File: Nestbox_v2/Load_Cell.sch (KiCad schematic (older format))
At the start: 29 parts

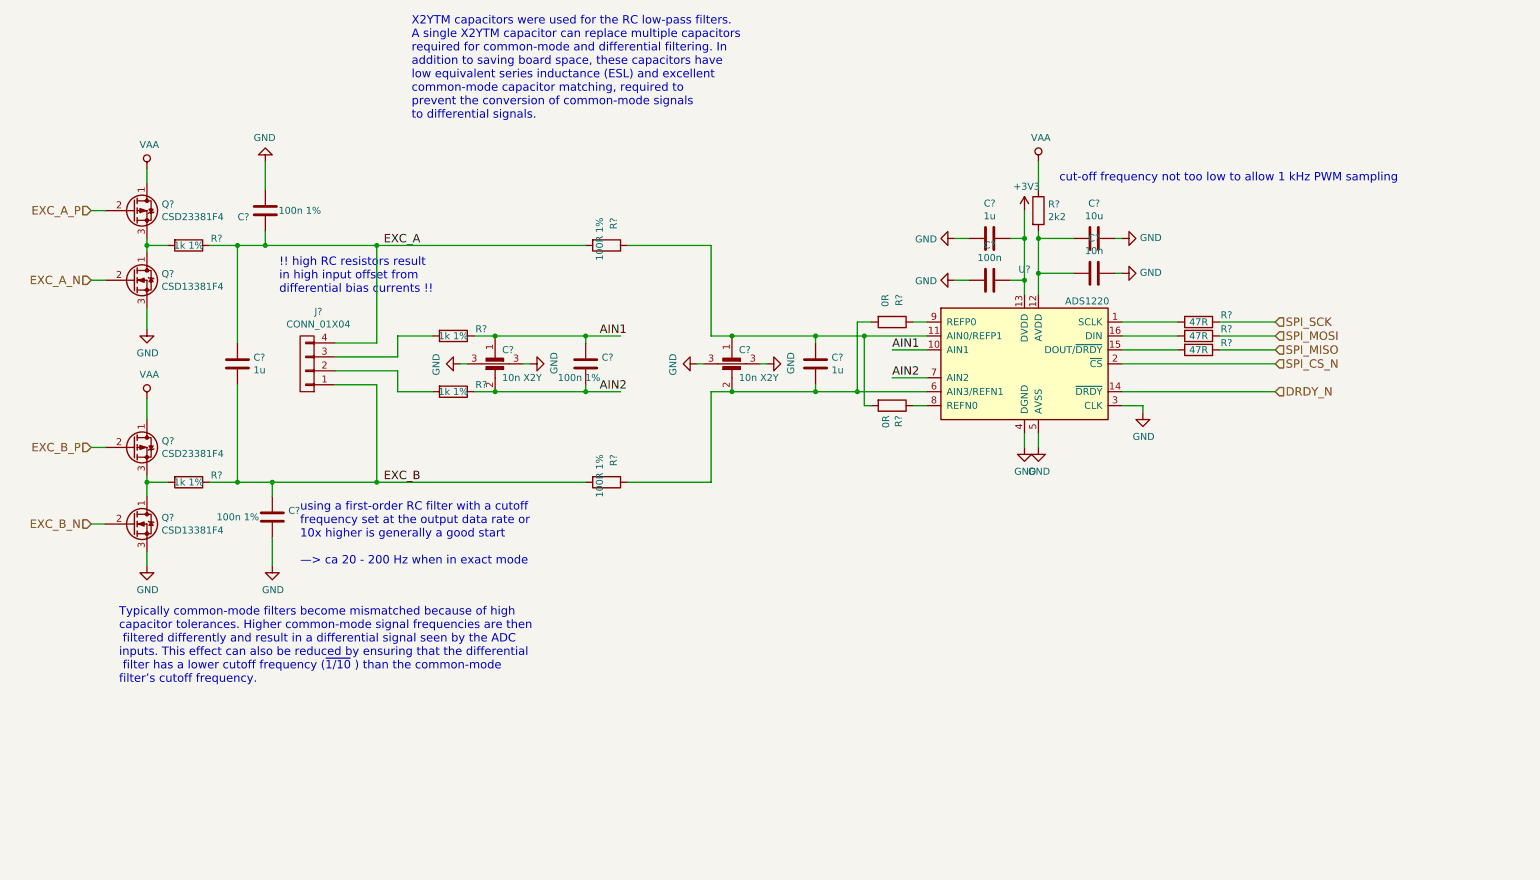
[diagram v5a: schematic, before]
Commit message: added PIR and lightbarrier headers
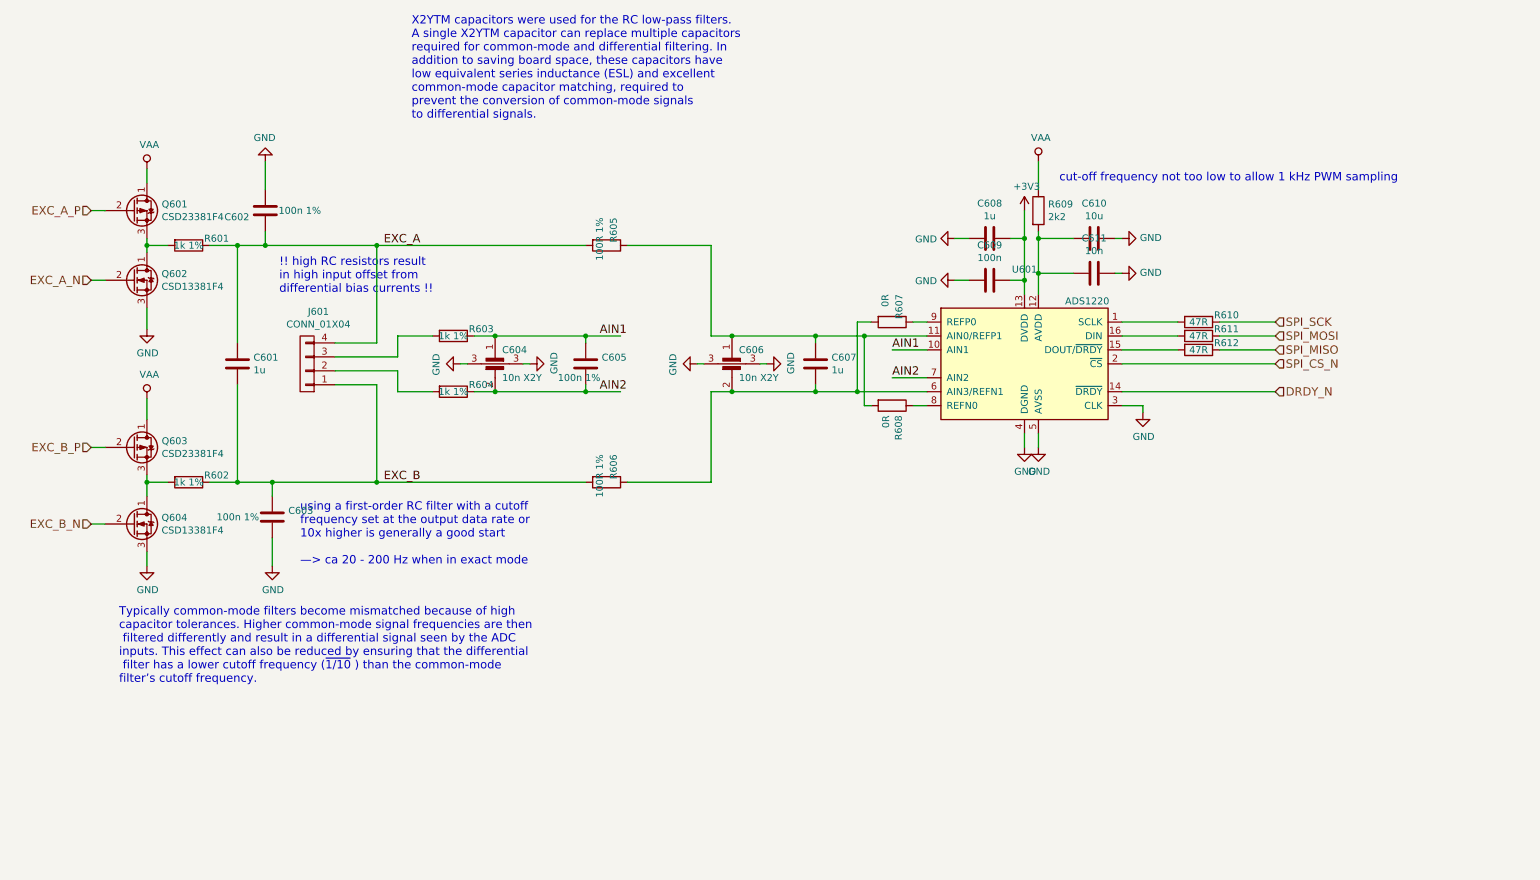
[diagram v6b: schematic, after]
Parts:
- gave numbers to parts that had none: 29

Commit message: added power footprints, final connector footprints
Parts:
- C601, C602, C603, C605, C607, C608, C609, C610, C611: footprint (none) -> Capacitors_SMD:C_0603
- C604, C606: footprint (none) -> murata-filter:NFM18PS
- J601: footprint (none) -> Terminal_Blocks:TerminalBlock_Pheonix_PT-3.5mm_4pol
- R601, R602, R603, R604, R605, R606, R607, R608, R609, R610, R611, R612: footprint (none) -> Resistors_SMD:R_0603
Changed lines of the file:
@@
 $Descr A4 11693 8268
 encoding utf-8
-Sheet 7 7
+Sheet 6 7
 Title ""
 Date ""
@@
 $EndDescr
 $Comp
-L +3V3 #PWR065
+L +3V3 #PWR066
 U 1 1 5AF731D8
 P 7950 2900
-F 0 "#PWR065" H 7950 2750 50  0001 C CNN
+F 0 "#PWR066" H 7950 2750 50  0001 C CNN
 F 1 "+3V3" H 7965 3073 50  0000 C CNN
 F 2 "" H 7950 2900 50  0001 C CNN
@@
 F 0 "R609" H 8120 2946 50  0000 L CNN
 F 1 "2k2" H 8120 2855 50  0000 L CNN
-F 2 "" V 7980 2900 50  0001 C CNN
+F 2 "Resistors_SMD:R_0603" V 7980 2900 50  0001 C CNN
 F 3 "" H 8050 2900 50  0001 C CNN
 	1    8050 2900
@@
 F 0 "C610" V 8198 3100 50  0000 C CNN
 F 1 "10u" V 8289 3100 50  0000 C CNN
-F 2 "" H 8488 2950 50  0001 C CNN
+F 2 "Capacitors_SMD:C_0603" H 8488 2950 50  0001 C CNN
 F 3 "" H 8450 3100 50  0001 C CNN
 	1    8450 3100
@@
 $EndComp
 $Comp
-L GND #PWR066
+L GND #PWR067
 U 1 1 5AF734D9
 P 7950 4600
-F 0 "#PWR066" H 7950 4350 50  0001 C CNN
+F 0 "#PWR067" H 7950 4350 50  0001 C CNN
 F 1 "GND" H 7955 4427 50  0000 C CNN
 F 2 "" H 7950 4600 50  0001 C CNN
@@
 F 0 "C609" V 7952 3400 50  0000 C CNN
 F 1 "100n" V 7861 3400 50  0000 C CNN
-F 2 "" H 7738 3250 50  0001 C CNN
+F 2 "Capacitors_SMD:C_0603" H 7738 3250 50  0001 C CNN
 F 3 "" H 7700 3400 50  0001 C CNN
 	1    7700 3400
@@
 F 0 "C608" V 7448 3100 50  0000 C CNN
 F 1 "1u" V 7539 3100 50  0000 C CNN
-F 2 "" H 7738 2950 50  0001 C CNN
+F 2 "Capacitors_SMD:C_0603" H 7738 2950 50  0001 C CNN
 F 3 "" H 7700 3100 50  0001 C CNN
 	1    7700 3100
@@
 F 0 "C611" V 8198 3350 50  0000 C CNN
 F 1 "10n" V 8289 3350 50  0000 C CNN
-F 2 "" H 8488 3200 50  0001 C CNN
+F 2 "Capacitors_SMD:C_0603" H 8488 3200 50  0001 C CNN
 F 3 "" H 8450 3350 50  0001 C CNN
 	1    8450 3350
@@
 $EndComp
 $Comp
-L GND #PWR067
+L GND #PWR068
 U 1 1 5AF737C3
 P 8050 4600
-F 0 "#PWR067" H 8050 4350 50  0001 C CNN
+F 0 "#PWR068" H 8050 4350 50  0001 C CNN
 F 1 "GND" H 8055 4427 50  0000 C CNN
 F 2 "" H 8050 4600 50  0001 C CNN
@@
 $EndComp
 $Comp
-L GND #PWR068
+L GND #PWR069
 U 1 1 5AF737DA
 P 8650 3100
-F 0 "#PWR068" H 8650 2850 50  0001 C CNN
+F 0 "#PWR069" H 8650 2850 50  0001 C CNN
 F 1 "GND" V 8655 2972 50  0000 R CNN
 F 2 "" H 8650 3100 50  0001 C CNN
@@
 $EndComp
 $Comp
-L GND #PWR069
+L GND #PWR070
 U 1 1 5AF73803
 P 8650 3350
-F 0 "#PWR069" H 8650 3100 50  0001 C CNN
+F 0 "#PWR070" H 8650 3100 50  0001 C CNN
 F 1 "GND" V 8655 3222 50  0000 R CNN
 F 2 "" H 8650 3350 50  0001 C CNN
@@
 $EndComp
 $Comp
-L GND #PWR070
+L GND #PWR071
 U 1 1 5AF73B67
 P 7450 3400
-F 0 "#PWR070" H 7450 3150 50  0001 C CNN
+F 0 "#PWR071" H 7450 3150 50  0001 C CNN
 F 1 "GND" V 7455 3272 50  0000 R CNN
 F 2 "" H 7450 3400 50  0001 C CNN
@@
 $EndComp
 $Comp
-L GND #PWR071
+L GND #PWR072
 U 1 1 5AF73BBF
 P 7450 3100
-F 0 "#PWR071" H 7450 2850 50  0001 C CNN
+F 0 "#PWR072" H 7450 2850 50  0001 C CNN
 F 1 "GND" V 7455 2972 50  0000 R CNN
 F 2 "" H 7450 3100 50  0001 C CNN
@@
 F 0 "C605" H 4915 4046 50  0000 L CNN
 F 1 "100n 1%" H 4600 3900 50  0000 L CNN
-F 2 "" H 4838 3850 50  0001 C CNN
+F 2 "Capacitors_SMD:C_0603" H 4838 3850 50  0001 C CNN
 F 3 "" H 4800 4000 50  0001 C CNN
 	1    4800 4000
@@
 F 0 "R603" V 3800 4000 50  0000 C CNN
 F 1 "1k 1%" V 3850 3800 50  0000 C CNN
-F 2 "" V 3780 3800 50  0001 C CNN
+F 2 "Resistors_SMD:R_0603" V 3780 3800 50  0001 C CNN
 F 3 "" H 3850 3800 50  0001 C CNN
 	1    3850 3800
@@
 F 0 "R604" V 3800 4400 50  0000 C CNN
 F 1 "1k 1%" V 3850 4200 50  0000 C CNN
-F 2 "" V 3780 4200 50  0001 C CNN
+F 2 "Resistors_SMD:R_0603" V 3780 4200 50  0001 C CNN
 F 3 "" H 3850 4200 50  0001 C CNN
 	1    3850 4200
@@
 F 0 "C607" H 6565 4046 50  0000 L CNN
 F 1 "1u" H 6565 3955 50  0000 L CNN
-F 2 "" H 6488 3850 50  0001 C CNN
+F 2 "Capacitors_SMD:C_0603" H 6488 3850 50  0001 C CNN
 F 3 "" H 6450 4000 50  0001 C CNN
 	1    6450 4000
@@
 $EndComp
 $Comp
-L GND #PWR072
+L GND #PWR073
 U 1 1 5AF756EC
 P 4400 4000
-F 0 "#PWR072" H 4400 3750 50  0001 C CNN
+F 0 "#PWR073" H 4400 3750 50  0001 C CNN
 F 1 "GND" H 4405 3827 50  0000 C CNN
 F 2 "" H 4400 4000 50  0001 C CNN
@@
 $EndComp
 $Comp
-L GND #PWR073
+L GND #PWR074
 U 1 1 5AF75761
 P 3900 4000
-F 0 "#PWR073" H 3900 3750 50  0001 C CNN
+F 0 "#PWR074" H 3900 3750 50  0001 C CNN
 F 1 "GND" H 3905 3827 50  0000 C CNN
 F 2 "" H 3900 4000 50  0001 C CNN
@@
 F 0 "J601" H 2719 3625 50  0000 C CNN
 F 1 "CONN_01X04" H 2719 3716 50  0000 C CNN
-F 2 "" H 2800 4000 50  0001 C CNN
+F 2 "Terminal_Blocks:TerminalBlock_Pheonix_PT-3.5mm_4pol" H 2800 4000 50  0001 C CNN
 F 3 "" H 2800 4000 50  0001 C CNN
 	1    2800 4000
@@
 F 0 "R612" V 9150 4100 50  0000 C CNN
 F 1 "47R" V 9200 3900 50  0000 C CNN
-F 2 "" V 9130 3900 50  0001 C CNN
+F 2 "Resistors_SMD:R_0603" V 9130 3900 50  0001 C CNN
 F 3 "" H 9200 3900 50  0001 C CNN
 	1    9200 3900
@@
 F 0 "R611" V 9150 4000 50  0000 C CNN
 F 1 "47R" V 9200 3800 50  0000 C CNN
-F 2 "" V 9130 3800 50  0001 C CNN
+F 2 "Resistors_SMD:R_0603" V 9130 3800 50  0001 C CNN
 F 3 "" H 9200 3800 50  0001 C CNN
 	1    9200 3800
@@
 F 0 "R610" V 9150 3900 50  0000 C CNN
 F 1 "47R" V 9200 3700 50  0000 C CNN
-F 2 "" V 9130 3700 50  0001 C CNN
+F 2 "Resistors_SMD:R_0603" V 9130 3700 50  0001 C CNN
 F 3 "" H 9200 3700 50  0001 C CNN
 	1    9200 3700
@@
 $EndComp
 $Comp
-L GND #PWR074
+L GND #PWR075
 U 1 1 5AF76892
 P 8800 4350
-F 0 "#PWR074" H 8800 4100 50  0001 C CNN
+F 0 "#PWR075" H 8800 4100 50  0001 C CNN
 F 1 "GND" H 8805 4177 50  0000 C CNN
 F 2 "" H 8800 4350 50  0001 C CNN
@@
 $EndComp
 $Comp
-L GND #PWR075
+L GND #PWR076
 U 1 1 5AF8B9E6
 P 1650 3750
-F 0 "#PWR075" H 1650 3500 50  0001 C CNN
+F 0 "#PWR076" H 1650 3500 50  0001 C CNN
 F 1 "GND" H 1655 3577 50  0000 C CNN
 F 2 "" H 1650 3750 50  0001 C CNN
@@
 $EndComp
 $Comp
-L GND #PWR076
+L GND #PWR077
 U 1 1 5AF8BA1F
 P 1650 5450
-F 0 "#PWR076" H 1650 5200 50  0001 C CNN
+F 0 "#PWR077" H 1650 5200 50  0001 C CNN
 F 1 "GND" H 1655 5277 50  0000 C CNN
 F 2 "" H 1650 5450 50  0001 C CNN
@@
 $EndComp
 $Comp
-L VAA #PWR077
+L VAA #PWR078
 U 1 1 5AF8BE8C
 P 1650 2600
-F 0 "#PWR077" H 1650 2450 50  0001 C CNN
+F 0 "#PWR078" H 1650 2450 50  0001 C CNN
 F 1 "VAA" H 1667 2773 50  0000 C CNN
 F 2 "" H 1650 2600 50  0001 C CNN
@@
 $EndComp
 $Comp
-L VAA #PWR078
+L VAA #PWR079
 U 1 1 5AF8C0F0
 P 1650 4250
-F 0 "#PWR078" H 1650 4100 50  0001 C CNN
+F 0 "#PWR079" H 1650 4100 50  0001 C CNN
 F 1 "VAA" H 1667 4423 50  0000 C CNN
 F 2 "" H 1650 4250 50  0001 C CNN
@@
 $EndComp
 $Comp
-L VAA #PWR079
+L VAA #PWR080
 U 1 1 5AF8C129
 P 8050 2550
-F 0 "#PWR079" H 8050 2400 50  0001 C CNN
+F 0 "#PWR080" H 8050 2400 50  0001 C CNN
 F 1 "VAA" H 8067 2723 50  0000 C CNN
 F 2 "" H 8050 2550 50  0001 C CNN
@@
 F 0 "R601" V 1900 3350 50  0000 C CNN
 F 1 "1k 1%" V 1950 3150 50  0000 C CNN
-F 2 "" V 1880 3150 50  0001 C CNN
+F 2 "Resistors_SMD:R_0603" V 1880 3150 50  0001 C CNN
 F 3 "" H 1950 3150 50  0001 C CNN
 	1    1950 3150
@@
 F 0 "R602" V 1900 5050 50  0000 C CNN
 F 1 "1k 1%" V 1950 4850 50  0000 C CNN
-F 2 "" V 1880 4850 50  0001 C CNN
+F 2 "Resistors_SMD:R_0603" V 1880 4850 50  0001 C CNN
 F 3 "" H 1950 4850 50  0001 C CNN
 	1    1950 4850
@@
 F 0 "C602" H 2615 2946 50  0000 L CNN
 F 1 "100n 1%" H 2100 2900 50  0000 L CNN
-F 2 "" H 2538 2750 50  0001 C CNN
+F 2 "Capacitors_SMD:C_0603" H 2538 2750 50  0001 C CNN
 F 3 "" H 2500 2900 50  0001 C CNN
 	1    2500 2900
@@
 F 0 "C603" H 2665 5146 50  0000 L CNN
 F 1 "100n 1%" H 2150 5100 50  0000 L CNN
-F 2 "" H 2588 4950 50  0001 C CNN
+F 2 "Capacitors_SMD:C_0603" H 2588 4950 50  0001 C CNN
 F 3 "" H 2550 5100 50  0001 C CNN
 	1    2550 5100
@@
 F 0 "C601" H 2415 4046 50  0000 L CNN
 F 1 "1u" H 2415 3955 50  0000 L CNN
-F 2 "" H 2338 3850 50  0001 C CNN
+F 2 "Capacitors_SMD:C_0603" H 2338 3850 50  0001 C CNN
 F 3 "" H 2300 4000 50  0001 C CNN
 	1    2300 4000
@@
 $EndComp
 $Comp
-L GND #PWR080
+L GND #PWR081
 U 1 1 5AF8D573
 P 2550 5450
-F 0 "#PWR080" H 2550 5200 50  0001 C CNN
+F 0 "#PWR081" H 2550 5200 50  0001 C CNN
 F 1 "GND" H 2555 5277 50  0000 C CNN
 F 2 "" H 2550 5450 50  0001 C CNN
@@
 $EndComp
 $Comp
-L GND #PWR081
+L GND #PWR082
 U 1 1 5AF8D7AF
 P 2500 2550
-F 0 "#PWR081" H 2500 2300 50  0001 C CNN
+F 0 "#PWR082" H 2500 2300 50  0001 C CNN
 F 1 "GND" H 2505 2377 50  0000 C CNN
 F 2 "" H 2500 2550 50  0001 C CNN
@@
 F 0 "R608" H 7070 4346 50  0000 L CNN
 F 1 "0R" H 7070 4255 50  0000 L CNN
-F 2 "" V 6930 4300 50  0001 C CNN
+F 2 "Resistors_SMD:R_0603" V 6930 4300 50  0001 C CNN
 F 3 "" H 7000 4300 50  0001 C CNN
 	1    7000 4300
@@
 F 0 "R607" H 6800 3750 50  0000 L CNN
 F 1 "0R" H 6800 3650 50  0000 L CNN
-F 2 "" V 6930 3700 50  0001 C CNN
+F 2 "Resistors_SMD:R_0603" V 6930 3700 50  0001 C CNN
 F 3 "" H 7000 3700 50  0001 C CNN
 	1    7000 3700
@@
 F 0 "C604" H 4200 4300 50  0000 L CNN
 F 1 "10n X2Y" H 4200 4100 50  0000 L CNN
-F 2 "" V 4150 4100 50  0001 C CNN
+F 2 "murata-filter:NFM18PS" V 4150 4100 50  0001 C CNN
 F 3 "" V 4150 4100 50  0001 C CNN
 	1    4150 4100
@@
 F 0 "C606" H 5900 4300 50  0000 L CNN
 F 1 "10n X2Y" H 5900 4100 50  0000 L CNN
-F 2 "" V 5850 4100 50  0001 C CNN
+F 2 "murata-filter:NFM18PS" V 5850 4100 50  0001 C CNN
 F 3 "" V 5850 4100 50  0001 C CNN
 	1    5850 4100
@@
 $EndComp
 $Comp
-L GND #PWR082
+L GND #PWR083
 U 1 1 5AF97D06
 P 6100 4000
-F 0 "#PWR082" H 6100 3750 50  0001 C CNN
+F 0 "#PWR083" H 6100 3750 50  0001 C CNN
 F 1 "GND" H 6105 3827 50  0000 C CNN
 F 2 "" H 6100 4000 50  0001 C CNN
@@
 $EndComp
 $Comp
-L GND #PWR083
+L GND #PWR084
 U 1 1 5AF97F53
 P 5600 4000
-F 0 "#PWR083" H 5600 3750 50  0001 C CNN
+F 0 "#PWR084" H 5600 3750 50  0001 C CNN
 F 1 "GND" H 5605 3827 50  0000 C CNN
 F 2 "" H 5600 4000 50  0001 C CNN
@@
 F 0 "R605" H 4750 3200 50  0000 L CNN
 F 1 "100R 1%" H 4750 3100 50  0000 L CNN
-F 2 "" V 4880 3150 50  0001 C CNN
+F 2 "Resistors_SMD:R_0603" V 4880 3150 50  0001 C CNN
 F 3 "" H 4950 3150 50  0001 C CNN
 	1    4950 3150
@@
 F 0 "R606" H 4750 4900 50  0000 L CNN
 F 1 "100R 1%" H 4750 4800 50  0000 L CNN
-F 2 "" V 4880 4850 50  0001 C CNN
+F 2 "Resistors_SMD:R_0603" V 4880 4850 50  0001 C CNN
 F 3 "" H 4950 4850 50  0001 C CNN
 	1    4950 4850

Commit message: correct size of the PCB drawn with connector arrangement done as well
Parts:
- J601: value CONN_01X04 -> LOAD_CELL_CONN_01X04
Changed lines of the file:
@@
 $EndDescr
 $Comp
-L +3V3 #PWR066
+L +3V3 #PWR613
 U 1 1 5AF731D8
 P 7950 2900
-F 0 "#PWR066" H 7950 2750 50  0001 C CNN
+F 0 "#PWR613" H 7950 2750 50  0001 C CNN
 F 1 "+3V3" H 7965 3073 50  0000 C CNN
 F 2 "" H 7950 2900 50  0001 C CNN
@@
 $EndComp
 $Comp
-L GND #PWR067
+L GND #PWR614
 U 1 1 5AF734D9
 P 7950 4600
-F 0 "#PWR067" H 7950 4350 50  0001 C CNN
+F 0 "#PWR614" H 7950 4350 50  0001 C CNN
 F 1 "GND" H 7955 4427 50  0000 C CNN
 F 2 "" H 7950 4600 50  0001 C CNN
@@
 $EndComp
 $Comp
-L GND #PWR068
+L GND #PWR616
 U 1 1 5AF737C3
 P 8050 4600
-F 0 "#PWR068" H 8050 4350 50  0001 C CNN
+F 0 "#PWR616" H 8050 4350 50  0001 C CNN
 F 1 "GND" H 8055 4427 50  0000 C CNN
 F 2 "" H 8050 4600 50  0001 C CNN
@@
 $EndComp
 $Comp
-L GND #PWR069
+L GND #PWR617
 U 1 1 5AF737DA
 P 8650 3100
-F 0 "#PWR069" H 8650 2850 50  0001 C CNN
+F 0 "#PWR617" H 8650 2850 50  0001 C CNN
 F 1 "GND" V 8655 2972 50  0000 R CNN
 F 2 "" H 8650 3100 50  0001 C CNN
@@
 $EndComp
 $Comp
-L GND #PWR070
+L GND #PWR618
 U 1 1 5AF73803
 P 8650 3350
-F 0 "#PWR070" H 8650 3100 50  0001 C CNN
+F 0 "#PWR618" H 8650 3100 50  0001 C CNN
 F 1 "GND" V 8655 3222 50  0000 R CNN
 F 2 "" H 8650 3350 50  0001 C CNN
@@
 $EndComp
 $Comp
-L GND #PWR071
+L GND #PWR612
 U 1 1 5AF73B67
 P 7450 3400
-F 0 "#PWR071" H 7450 3150 50  0001 C CNN
+F 0 "#PWR612" H 7450 3150 50  0001 C CNN
 F 1 "GND" V 7455 3272 50  0000 R CNN
 F 2 "" H 7450 3400 50  0001 C CNN
@@
 $EndComp
 $Comp
-L GND #PWR072
+L GND #PWR611
 U 1 1 5AF73BBF
 P 7450 3100
-F 0 "#PWR072" H 7450 2850 50  0001 C CNN
+F 0 "#PWR611" H 7450 2850 50  0001 C CNN
 F 1 "GND" V 7455 2972 50  0000 R CNN
 F 2 "" H 7450 3100 50  0001 C CNN
@@
 $EndComp
 $Comp
-L GND #PWR073
+L GND #PWR608
 U 1 1 5AF756EC
 P 4400 4000
-F 0 "#PWR073" H 4400 3750 50  0001 C CNN
+F 0 "#PWR608" H 4400 3750 50  0001 C CNN
 F 1 "GND" H 4405 3827 50  0000 C CNN
 F 2 "" H 4400 4000 50  0001 C CNN
@@
 $EndComp
 $Comp
-L GND #PWR074
+L GND #PWR607
 U 1 1 5AF75761
 P 3900 4000
-F 0 "#PWR074" H 3900 3750 50  0001 C CNN
+F 0 "#PWR607" H 3900 3750 50  0001 C CNN
 F 1 "GND" H 3905 3827 50  0000 C CNN
 F 2 "" H 3900 4000 50  0001 C CNN
@@
 P 2800 4000
 F 0 "J601" H 2719 3625 50  0000 C CNN
-F 1 "CONN_01X04" H 2719 3716 50  0000 C CNN
+F 1 "LOAD_CELL_CONN_01X04" H 2719 3716 50  0000 C CNN
 F 2 "Terminal_Blocks:TerminalBlock_Pheonix_PT-3.5mm_4pol" H 2800 4000 50  0001 C CNN
 F 3 "" H 2800 4000 50  0001 C CNN
@@
 $EndComp
 $Comp
-L GND #PWR075
+L GND #PWR619
 U 1 1 5AF76892
 P 8800 4350
-F 0 "#PWR075" H 8800 4100 50  0001 C CNN
+F 0 "#PWR619" H 8800 4100 50  0001 C CNN
 F 1 "GND" H 8805 4177 50  0000 C CNN
 F 2 "" H 8800 4350 50  0001 C CNN
@@
 $EndComp
 $Comp
-L GND #PWR076
+L GND #PWR602
 U 1 1 5AF8B9E6
 P 1650 3750
-F 0 "#PWR076" H 1650 3500 50  0001 C CNN
+F 0 "#PWR602" H 1650 3500 50  0001 C CNN
 F 1 "GND" H 1655 3577 50  0000 C CNN
 F 2 "" H 1650 3750 50  0001 C CNN
@@
 $EndComp
 $Comp
-L GND #PWR077
+L GND #PWR604
 U 1 1 5AF8BA1F
 P 1650 5450
-F 0 "#PWR077" H 1650 5200 50  0001 C CNN
+F 0 "#PWR604" H 1650 5200 50  0001 C CNN
 F 1 "GND" H 1655 5277 50  0000 C CNN
 F 2 "" H 1650 5450 50  0001 C CNN
@@
 $EndComp
 $Comp
-L VAA #PWR078
+L VAA #PWR601
 U 1 1 5AF8BE8C
 P 1650 2600
-F 0 "#PWR078" H 1650 2450 50  0001 C CNN
+F 0 "#PWR601" H 1650 2450 50  0001 C CNN
 F 1 "VAA" H 1667 2773 50  0000 C CNN
 F 2 "" H 1650 2600 50  0001 C CNN
@@
 $EndComp
 $Comp
-L VAA #PWR079
+L VAA #PWR603
 U 1 1 5AF8C0F0
 P 1650 4250
-F 0 "#PWR079" H 1650 4100 50  0001 C CNN
+F 0 "#PWR603" H 1650 4100 50  0001 C CNN
 F 1 "VAA" H 1667 4423 50  0000 C CNN
 F 2 "" H 1650 4250 50  0001 C CNN
@@
 $EndComp
 $Comp
-L VAA #PWR080
+L VAA #PWR615
 U 1 1 5AF8C129
 P 8050 2550
-F 0 "#PWR080" H 8050 2400 50  0001 C CNN
+F 0 "#PWR615" H 8050 2400 50  0001 C CNN
 F 1 "VAA" H 8067 2723 50  0000 C CNN
 F 2 "" H 8050 2550 50  0001 C CNN
@@
 $EndComp
 $Comp
-L GND #PWR081
+L GND #PWR606
 U 1 1 5AF8D573
 P 2550 5450
-F 0 "#PWR081" H 2550 5200 50  0001 C CNN
+F 0 "#PWR606" H 2550 5200 50  0001 C CNN
 F 1 "GND" H 2555 5277 50  0000 C CNN
 F 2 "" H 2550 5450 50  0001 C CNN
@@
 $EndComp
 $Comp
-L GND #PWR082
+L GND #PWR605
 U 1 1 5AF8D7AF
 P 2500 2550
-F 0 "#PWR082" H 2500 2300 50  0001 C CNN
+F 0 "#PWR605" H 2500 2300 50  0001 C CNN
 F 1 "GND" H 2505 2377 50  0000 C CNN
 F 2 "" H 2500 2550 50  0001 C CNN
@@
 $EndComp
 $Comp
-L GND #PWR083
+L GND #PWR610
 U 1 1 5AF97D06
 P 6100 4000
-F 0 "#PWR083" H 6100 3750 50  0001 C CNN
+F 0 "#PWR610" H 6100 3750 50  0001 C CNN
 F 1 "GND" H 6105 3827 50  0000 C CNN
 F 2 "" H 6100 4000 50  0001 C CNN
@@
 $EndComp
 $Comp
-L GND #PWR084
+L GND #PWR609
 U 1 1 5AF97F53
 P 5600 4000
-F 0 "#PWR084" H 5600 3750 50  0001 C CNN
+F 0 "#PWR609" H 5600 3750 50  0001 C CNN
 F 1 "GND" H 5605 3827 50  0000 C CNN
 F 2 "" H 5600 4000 50  0001 C CNN
